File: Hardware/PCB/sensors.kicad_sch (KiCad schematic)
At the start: 26 parts, among them IC3 MPX5500DP, IC4 MPX5500DP, U2 ADS1219IPWR, U6 TPS7A2050PDBVR

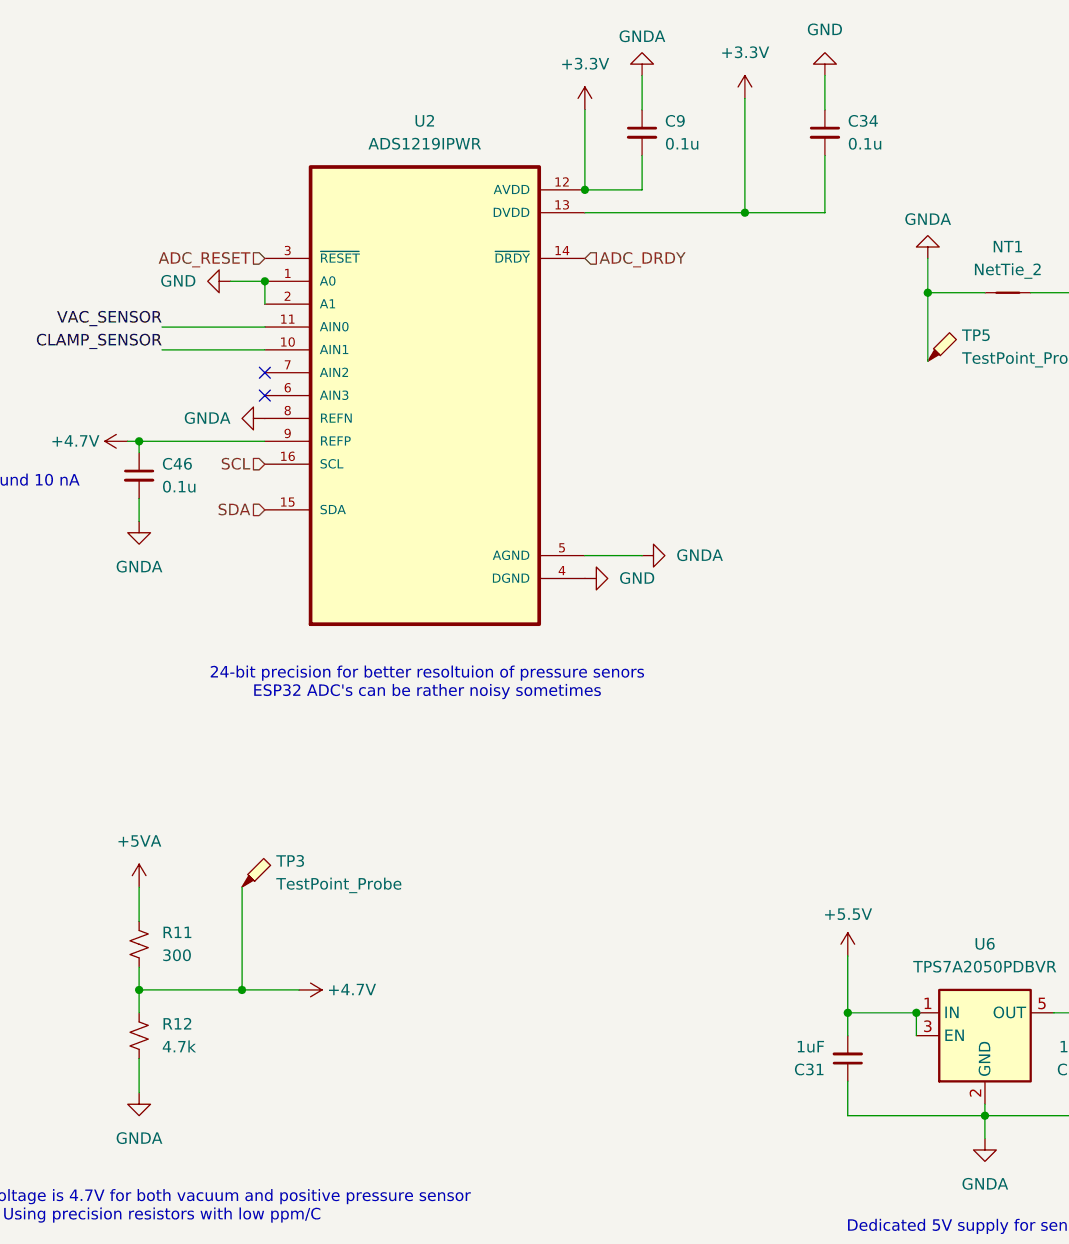
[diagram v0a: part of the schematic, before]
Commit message: fixed BOM, added some silkscreen, getting quote now
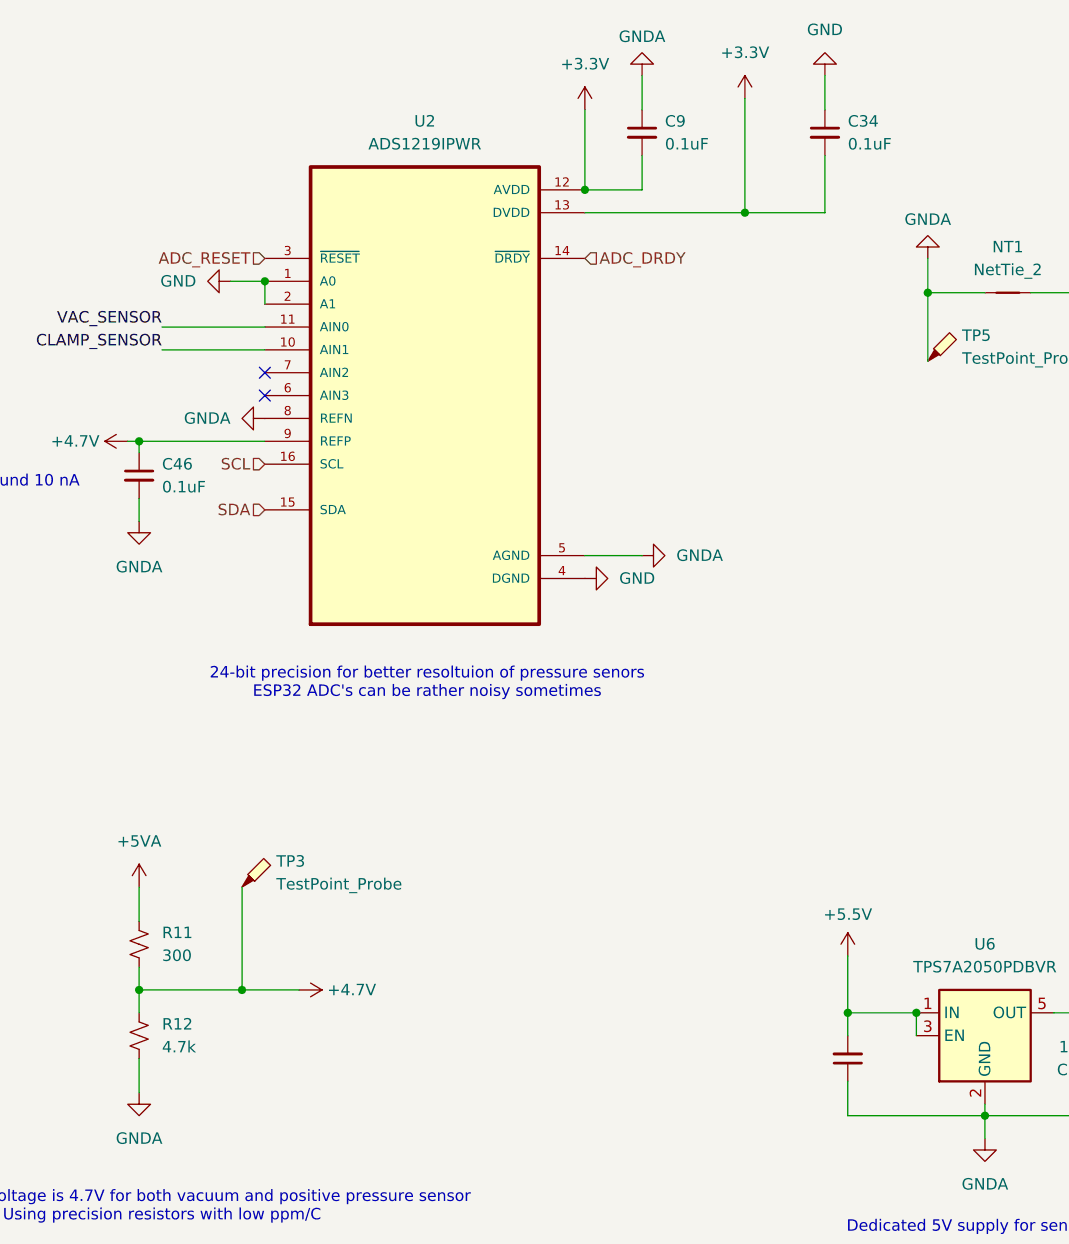
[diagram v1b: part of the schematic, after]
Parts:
- C31, C32: DigiKey Link (none) -> https://www.digikey.com/en/products/detail/samsung-electro-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; MPN (none) -> CL10B105KO8NNNC; Manufacturer (none) -> Samsung Electro-Mechanics
- C34, C46, C9: value 0.1u -> 0.1uF
- TP3, TP4, TP5, TP6: now left out of the parts list
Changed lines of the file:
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@@
 		(unit 1)
 		(exclude_from_sim no)
-		(in_bom yes)
+		(in_bom no)
 		(on_board yes)
 		(dnp no)
@@
 		(on_board yes)
 		(dnp no)
-		(fields_autoplaced yes)
 		(property "Reference" "C32"
 			(at 259.08 135.8838 0)
@@
 			)
 		)
-		(property "Description" "Unpolarized capacitor, small symbol"
+		(property "Description" "1 µF ±10% 16V Ceramic Capacitor X7R 0603 (1608 Metric)"
+			(at 261.62 134.62 0)
+			(effects
+				(font
+					(size 1.27 1.27)
+				)
+				(hide yes)
+			)
+		)
+		(property "DigiKey Link" "https://www.digikey.com/en/products/detail/samsung-electro-mechanics/CL10B105KO8NNNC/3886677"
+			(at 261.62 134.62 0)
+			(effects
+				(font
+					(size 1.27 1.27)
+				)
+				(hide yes)
+			)
+		)
+		(property "MPN" "CL10B105KO8NNNC"
+			(at 261.62 134.62 0)
+			(effects
+				(font
+					(size 1.27 1.27)
+				)
+				(hide yes)
+			)
+		)
+		(property "Manufacturer" "Samsung Electro-Mechanics"
+			(at 261.62 134.62 0)
+			(effects
+				(font
+					(size 1.27 1.27)
+				)
+				(hide yes)
+			)
+		)
+		(property "Mouser Link" ""
 			(at 261.62 134.62 0)
 			(effects
@@
 			)
 		)
-		(property "Value" "0.1u"
+		(property "Value" "0.1uF"
 			(at 212.09 33.0262 0)
 			(effects
@@
 			)
 		)
-		(property "Value" "0.1u"
+		(property "Value" "0.1uF"
 			(at 232.41 33.0262 0)
 			(effects
@@
 			)
 		)
-		(property "Value" "0.1u"
+		(property "Value" "0.1uF"
 			(at 156.21 71.1262 0)
 			(effects
@@
 		(on_board yes)
 		(dnp no)
-		(fields_autoplaced yes)
 		(property "Reference" "C31"
 			(at 229.87 135.8838 0)
@@
 				)
 				(justify left)
+				(hide yes)
 			)
 		)
@@
 				)
 				(justify left)
+				(hide yes)
 			)
 		)
@@
 			)
 		)
-		(property "Description" "Unpolarized capacitor, small symbol"
+		(property "Description" "1 µF ±10% 16V Ceramic Capacitor X7R 0603 (1608 Metric)"
+			(at 232.41 134.62 0)
+			(effects
+				(font
+					(size 1.27 1.27)
+				)
+				(hide yes)
+			)
+		)
+		(property "DigiKey Link" "https://www.digikey.com/en/products/detail/samsung-electro-mechanics/CL10B105KO8NNNC/3886677"
+			(at 232.41 134.62 0)
+			(effects
+				(font
+					(size 1.27 1.27)
+				)
+				(hide yes)
+			)
+		)
+		(property "MPN" "CL10B105KO8NNNC"
+			(at 232.41 134.62 0)
+			(effects
+				(font
+					(size 1.27 1.27)
+				)
+				(hide yes)
+			)
+		)
+		(property "Manufacturer" "Samsung Electro-Mechanics"
+			(at 232.41 134.62 0)
+			(effects
+				(font
+					(size 1.27 1.27)
+				)
+				(hide yes)
+			)
+		)
+		(property "Mouser Link" ""
 			(at 232.41 134.62 0)
 			(effects
@@
 		(unit 1)
 		(exclude_from_sim no)
-		(in_bom yes)
+		(in_bom no)
 		(on_board yes)
 		(dnp no)
@@
 		(unit 1)
 		(exclude_from_sim no)
-		(in_bom yes)
+		(in_bom no)
 		(on_board yes)
 		(dnp no)
@@
 		(unit 1)
 		(exclude_from_sim no)
-		(in_bom yes)
-		(on_board yes)
-		(dnp no)
+		(in_bom no)
+		(on_board yes)
+		(dnp no)

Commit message: kinda pricey, I should try to make a smaller version using LCSC parts for cheaper solution
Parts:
- C17, C29, C31, C32: LCSC (none) -> C59782
- C19, C30: LCSC (none) -> C15195
- C20, C28: LCSC (none) -> C27694
- C34, C46, C9: LCSC (none) -> C66501
- C37, C38: LCSC (none) -> C159798
- IC3, IC4: LCSC (none) -> C410771
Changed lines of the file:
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@@
 		(polyline
 			(pts
-				(xy 20.32 34.29) (xy 20.32 86.36) (xy 110.49 86.36) (xy 111.76 85.09) (xy 111.76 34.29)
+				(xy 21.59 113.03) (xy 21.59 165.1) (xy 111.76 165.1) (xy 113.03 163.83) (xy 113.03 113.03)
 			)
 			(stroke
@@
 		(polyline
 			(pts
-				(xy 21.59 113.03) (xy 21.59 165.1) (xy 111.76 165.1) (xy 113.03 163.83) (xy 113.03 113.03)
+				(xy 20.32 34.29) (xy 20.32 86.36) (xy 110.49 86.36) (xy 111.76 85.09) (xy 111.76 34.29)
 			)
 			(stroke
@@
 			)
 		)
+		(property "LCSC" ""
+			(at 153.67 132.08 0)
+			(effects
+				(font
+					(size 1.27 1.27)
+				)
+			)
+		)
 		(pin "2"
 		)
@@
 			)
 		)
+		(property "LCSC" "C15195"
+			(at 64.77 129.54 0)
+			(effects
+				(font
+					(size 1.27 1.27)
+				)
+			)
+		)
 		(pin "1"
 		)
@@
 			)
 		)
+		(property "LCSC" "C159798"
+			(at 77.47 149.86 0)
+			(effects
+				(font
+					(size 1.27 1.27)
+				)
+			)
+		)
 		(pin "1"
 		)
@@
 			)
 		)
+		(property "LCSC" ""
+			(at 165.1 115.57 0)
+			(effects
+				(font
+					(size 1.27 1.27)
+				)
+			)
+		)
 		(pin "1"
 		)
@@
 			)
 		)
+		(property "LCSC" ""
+			(at 247.65 132.08 0)
+			(effects
+				(font
+					(size 1.27 1.27)
+				)
+			)
+		)
 		(pin "3"
 		)
@@
 			)
 		)
+		(property "LCSC" "C15195"
+			(at 62.23 49.53 0)
+			(effects
+				(font
+					(size 1.27 1.27)
+				)
+			)
+		)
 		(pin "1"
 		)
@@
 			)
 		)
+		(property "LCSC" "C59782"
+			(at 57.15 129.54 0)
+			(effects
+				(font
+					(size 1.27 1.27)
+				)
+			)
+		)
 		(pin "1"
 		)
@@
 			)
 		)
+		(property "LCSC" "C59782"
+			(at 261.62 134.62 0)
+			(effects
+				(font
+					(size 1.27 1.27)
+				)
+			)
+		)
 		(pin "1"
 		)
@@
 			)
 		)
+		(property "LCSC" "C66501"
+			(at 209.55 31.75 0)
+			(effects
+				(font
+					(size 1.27 1.27)
+				)
+			)
+		)
 		(pin "2"
 		)
@@
 			)
 		)
+		(property "LCSC" ""
+			(at 67.31 143.51 0)
+			(effects
+				(font
+					(size 1.27 1.27)
+				)
+			)
+		)
 		(pin "2"
 		)
@@
 			)
 		)
+		(property "LCSC" ""
+			(at 153.67 121.92 0)
+			(effects
+				(font
+					(size 1.27 1.27)
+				)
+			)
+		)
 		(pin "2"
 		)
@@
 			)
 		)
+		(property "LCSC" "C410771"
+			(at 45.72 143.51 0)
+			(effects
+				(font
+					(size 1.27 1.27)
+				)
+			)
+		)
 		(pin "3"
 		)
@@
 			)
 		)
+		(property "LCSC" "C66501"
+			(at 229.87 31.75 0)
+			(effects
+				(font
+					(size 1.27 1.27)
+				)
+			)
+		)
 		(pin "2"
 		)
@@
 			)
 		)
+		(property "LCSC" ""
+			(at 250.19 49.53 0)
+			(effects
+				(font
+					(size 1.27 1.27)
+				)
+			)
+		)
 		(pin "2"
 		)
@@
 			)
 		)
+		(property "LCSC" "C66501"
+			(at 153.67 69.85 0)
+			(effects
+				(font
+					(size 1.27 1.27)
+				)
+			)
+		)
 		(pin "2"
 		)
@@
 			)
 		)
+		(property "LCSC" "C410771"
+			(at 43.18 63.5 0)
+			(effects
+				(font
+					(size 1.27 1.27)
+				)
+			)
+		)
 		(pin "3"
 		)
@@
 			)
 		)
+		(property "LCSC" "C159798"
+			(at 74.93 69.85 0)
+			(effects
+				(font
+					(size 1.27 1.27)
+				)
+			)
+		)
 		(pin "1"
 		)
@@
 			)
 		)
+		(property "LCSC" "C27694"
+			(at 54.61 149.86 0)
+			(effects
+				(font
+					(size 1.27 1.27)
+				)
+			)
+		)
 		(pin "1"
 		)
@@
 				)
 				(justify left)
-				(hide yes)
 			)
 		)
@@
 				)
 				(justify left)
-				(hide yes)
 			)
 		)
@@
 			)
 		)
+		(property "LCSC" "C59782"
+			(at 232.41 134.62 0)
+			(effects
+				(font
+					(size 1.27 1.27)
+				)
+			)
+		)
 		(pin "1"
 		)
@@
 			)
 		)
+		(property "LCSC" "C27694"
+			(at 52.07 69.85 0)
+			(effects
+				(font
+					(size 1.27 1.27)
+				)
+			)
+		)
 		(pin "1"
 		)
@@
 			)
 		)
+		(property "LCSC" "C59782"
+			(at 54.61 49.53 0)
+			(effects
+				(font
+					(size 1.27 1.27)
+				)
+			)
+		)
 		(pin "1"
 		)
@@
 			)
 		)
+		(property "LCSC" ""
+			(at 88.9 154.94 0)
+			(effects
+				(font
+					(size 1.27 1.27)
+				)
+			)
+		)
 		(pin "1"
 		)
@@
 			)
 		)
+		(property "LCSC" ""
+			(at 86.36 74.93 0)
+			(effects
+				(font
+					(size 1.27 1.27)
+				)
+			)
+		)
 		(pin "1"
 		)
@@
 			)
 		)
+		(property "LCSC" ""
+			(at 241.3 57.15 0)
+			(effects
+				(font
+					(size 1.27 1.27)
+				)
+			)
+		)
 		(pin "1"
 		)
@@
 			)
 		)
+		(property "LCSC" ""
+			(at 64.77 63.5 0)
+			(effects
+				(font
+					(size 1.27 1.27)
+				)
+			)
+		)
 		(pin "2"
 		)
@@
 			)
 		)
+		(property "LCSC" ""
+			(at 185.42 60.96 0)
+			(effects
+				(font
+					(size 1.27 1.27)
+				)
+			)
+		)

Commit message: done with this, placed order
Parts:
- removed C17, C29: 1uF, Capacitor_SMD:C_0603_1608Metric_Pad1.08x0.95mm_HandSolder, symbol Device:C_Small
- removed C19, C30: 0.01uF, Capacitor_SMD:C_0402_1005Metric_Pad0.74x0.62mm_HandSolder, symbol Device:C_Small
- removed C20, C28: 470pF, Capacitor_SMD:C_0603_1608Metric_Pad1.08x0.95mm_HandSolder, symbol Device:C_Small
- removed C34, C46, C9: 0.1uF, Capacitor_SMD:C_0603_1608Metric_Pad1.08x0.95mm_HandSolder, symbol Device:C_Small
- removed C37, C38: 0.33uF, Capacitor_SMD:C_0603_1608Metric_Pad1.08x0.95mm_HandSolder, symbol Device:C_Small
- removed IC3, IC4: MPX5500DP, Vendor_Footprints:MPX5500DP, symbol Vendor_Symbols:MPX5500DP
- removed R25, R26: 750, Resistor_SMD:R_0603_1608Metric_Pad0.98x0.95mm_HandSolder, symbol Device:R_Small_US
- removed TP4, TP5, TP6: TestPoint_Probe, TestPoint:TestPoint_Keystone_5000-5004_Miniature, symbol Connector:TestPoint_Probe
- removed U2: ADS1219IPWR, Vendor_Footprints:SOP65P640X120-16N, symbol Vendor_Symbols:ADS1219IPWR
- removed U6: TPS7A2050PDBVR, Package_TO_SOT_SMD:SOT-23-5, symbol Regulator_Linear:TPS7A0531PDBV
- added C10: 100nF, Capacitor_SMD:C_0603_1608Metric_Pad1.08x0.95mm_HandSolder, symbol Device:C_Small
- added C27: 0.01uF, Capacitor_SMD:C_0402_1005Metric_Pad0.74x0.62mm_HandSolder, symbol Device:C_Small
- added C41, C42: 1uF, Capacitor_SMD:C_0603_1608Metric_Pad1.08x0.95mm_HandSolder, symbol Device:C_Small
- added U4: SPX5205M5-L-5-0/TR, Package_TO_SOT_SMD:SOT-23-5, symbol Regulator_Linear:SPX3819M5-L-5-0
- added U6: ADS1232IPW, Package_SO:TSSOP-24_6.1x7.8mm_P0.65mm, symbol Analog_ADC:ADS1232IPW
- C31, C32: value 1uF -> 100nF; DigiKey Link https://www.digikey.com/en/products/detail/samsung-electro-mechanics/CL10B105KO8NNNC/3886677 -> https://www.digikey.com/en/products/detail/samsung-electro-mechanics/CL10B104KO8NNNC/3886663; LCSC C59782 -> C14663; MPN CL10B105KO8NNNC -> CC0603KRX7R9BB104; Manufacturer Samsung Electro-Mechanics -> YAGEO
- R11: LCSC (none) -> C705763; MPN RG1608P-301-B-T5 -> RT0603BRD07300RL; Manufacturer Susumu -> YAGEO
- R12: LCSC (none) -> C513565; MPN RG1608P-472-B-T5 -> RT0603BRD074K7L; Manufacturer Susumu -> YAGEO
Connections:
- net +3.3V: now also C32.1, U6.1 (DVDD)
- net +4.7V: now also U6.16 (REFP)
- net +5.5V: now also C42.2, U4.1 (IN), U4.3 (EN); no longer C31.2
- net +5VA: now also C31.1, C41.2, U4.5 (OUT), U6.18 (AVDD); no longer C32.2
- net GND: now also C32.2, C42.1, U4.2 (GND), U6.2 (DGND), U6.5 (DGND), U6.6 (DGND)
- net GNDA: now also C31.2, C27.1, C41.1, U6.12 (AINN1), U6.13 (AINN2), U6.15 (REFN), U6.17 (AGND), U6.19 (GAIN0), U6.20 (GAIN1), U6.3 (CLKIN/XTAL1), U6.7 (TEMP); no longer C31.1, C32.1
- new net: C27.2, U4.4 (BP)
- new net: C10.1, U6.9 (CAP)
- new net: C10.2, U6.10 (CAP)
- new net DOUT: U6.24 (~{DRDY}/DOUT)
- new net INPUT_MUX: U6.8 (A0)
- new net PWDN: U6.22 (~{PWDN})
- new net SCLK: U6.23 (SCLK)
- new net SPEED: U6.21 (SPEED)
- new net pressure_sensor/SENSOR_VOUT: U6.11 (AINP1)
- new net pressure_sensor1/SENSOR_VOUT: U6.14 (AINP2)
- no-connect marks 8 -> 1
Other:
- added sheet pressure_sensor (pressure_sensor.kicad_sch)
- added sheet pressure_sensor1 (pressure_sensor.kicad_sch)
- moved on the sheet: R11, R12, TP3
